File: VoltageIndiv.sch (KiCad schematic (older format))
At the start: 2 parts

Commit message: Placement canal passif intial
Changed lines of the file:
@@
 AR Path="/5F37413F/5EC90889" Ref="R79"  Part="1"
 AR Path="/5F374143/5EC90889" Ref="R81"  Part="1"
-F 0 "R81" H 5770 4046 50  0000 L CNN
+F 0 "R67" H 5770 4046 50  0000 L CNN
 F 1 "100k" H 5770 3955 50  0000 L CNN
 F 2 "Resistor_SMD:R_0805_2012Metric" V 5630 4000 50  0001 C CNN
@@
 AR Path="/5F37413F/5EC91EB2" Ref="R78"  Part="1"
 AR Path="/5F374143/5EC91EB2" Ref="R80"  Part="1"
-F 0 "R80" H 5770 3546 50  0000 L CNN
+F 0 "R66" H 5770 3546 50  0000 L CNN
 F 1 "43k" H 5770 3455 50  0000 L CNN
 F 2 "Resistor_SMD:R_0805_2012Metric" V 5630 3500 50  0001 C CNN
@@
 AR Path="/5F37413F/60F963CD" Ref="#PWR0138"  Part="1"
 AR Path="/5F374143/60F963CD" Ref="#PWR0139"  Part="1"
-F 0 "#PWR0139" H 5700 4050 50  0001 C CNN
+F 0 "#PWR0132" H 5700 4050 50  0001 C CNN
 F 1 "GNDA" H 5705 4127 50  0000 C CNN
 F 2 "" H 5700 4300 50  0001 C CNN

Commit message: Placement première charge active
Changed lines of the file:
@@
 $Descr A4 11693 8268
 encoding utf-8
-Sheet 35 80
+Sheet 41 80
 Title ""
 Date "2020-05-19"
@@
 AR Path="/5F37413F/5EC90889" Ref="R79"  Part="1"
 AR Path="/5F374143/5EC90889" Ref="R81"  Part="1"
-F 0 "R67" H 5770 4046 50  0000 L CNN
+F 0 "R81" H 5770 4046 50  0000 L CNN
 F 1 "100k" H 5770 3955 50  0000 L CNN
 F 2 "Resistor_SMD:R_0805_2012Metric" V 5630 4000 50  0001 C CNN
@@
 AR Path="/5F37413F/5EC91EB2" Ref="R78"  Part="1"
 AR Path="/5F374143/5EC91EB2" Ref="R80"  Part="1"
-F 0 "R66" H 5770 3546 50  0000 L CNN
+F 0 "R80" H 5770 3546 50  0000 L CNN
 F 1 "43k" H 5770 3455 50  0000 L CNN
 F 2 "Resistor_SMD:R_0805_2012Metric" V 5630 3500 50  0001 C CNN
@@
 AR Path="/5F37413F/60F963CD" Ref="#PWR0138"  Part="1"
 AR Path="/5F374143/60F963CD" Ref="#PWR0139"  Part="1"
-F 0 "#PWR0132" H 5700 4050 50  0001 C CNN
+F 0 "#PWR0139" H 5700 4050 50  0001 C CNN
 F 1 "GNDA" H 5705 4127 50  0000 C CNN
 F 2 "" H 5700 4300 50  0001 C CNN

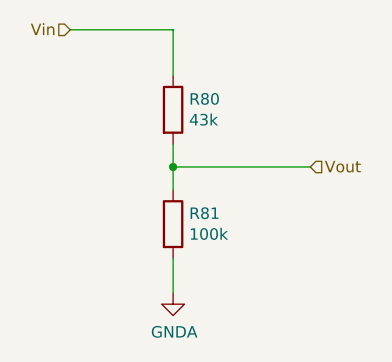
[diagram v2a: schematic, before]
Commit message: Placement première charge active 2nd try
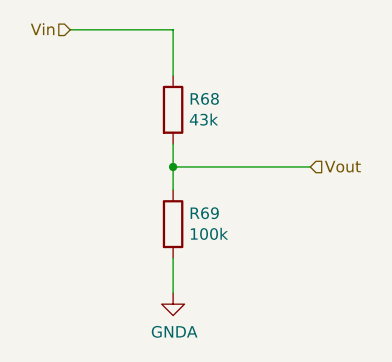
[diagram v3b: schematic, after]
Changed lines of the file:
@@
 $Descr A4 11693 8268
 encoding utf-8
-Sheet 41 80
+Sheet 36 80
 Title ""
 Date "2020-05-19"
@@
 AR Path="/5F37413F/5EC90889" Ref="R79"  Part="1"
 AR Path="/5F374143/5EC90889" Ref="R81"  Part="1"
-F 0 "R81" H 5770 4046 50  0000 L CNN
+F 0 "R69" H 5770 4046 50  0000 L CNN
 F 1 "100k" H 5770 3955 50  0000 L CNN
 F 2 "Resistor_SMD:R_0805_2012Metric" V 5630 4000 50  0001 C CNN
@@
 AR Path="/5F37413F/5EC91EB2" Ref="R78"  Part="1"
 AR Path="/5F374143/5EC91EB2" Ref="R80"  Part="1"
-F 0 "R80" H 5770 3546 50  0000 L CNN
+F 0 "R68" H 5770 3546 50  0000 L CNN
 F 1 "43k" H 5770 3455 50  0000 L CNN
 F 2 "Resistor_SMD:R_0805_2012Metric" V 5630 3500 50  0001 C CNN
@@
 AR Path="/5F37413F/60F963CD" Ref="#PWR0138"  Part="1"
 AR Path="/5F374143/60F963CD" Ref="#PWR0139"  Part="1"
-F 0 "#PWR0139" H 5700 4050 50  0001 C CNN
+F 0 "#PWR0133" H 5700 4050 50  0001 C CNN
 F 1 "GNDA" H 5705 4127 50  0000 C CNN
 F 2 "" H 5700 4300 50  0001 C CNN

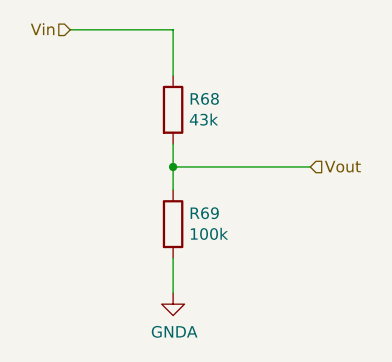
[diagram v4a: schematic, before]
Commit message: Petit ajustement pour accomoder le usb du arduino, pret pour routing
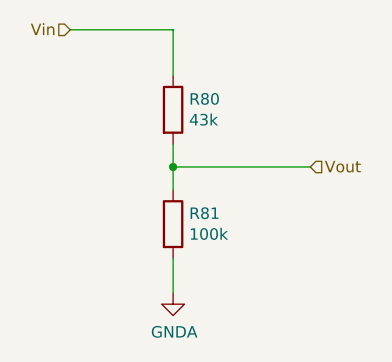
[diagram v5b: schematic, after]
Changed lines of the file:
@@
 AR Path="/5F37413F/5EC90889" Ref="R79"  Part="1"
 AR Path="/5F374143/5EC90889" Ref="R81"  Part="1"
-F 0 "R69" H 5770 4046 50  0000 L CNN
+F 0 "R81" H 5770 4046 50  0000 L CNN
 F 1 "100k" H 5770 3955 50  0000 L CNN
 F 2 "Resistor_SMD:R_0805_2012Metric" V 5630 4000 50  0001 C CNN
@@
 AR Path="/5F37413F/5EC91EB2" Ref="R78"  Part="1"
 AR Path="/5F374143/5EC91EB2" Ref="R80"  Part="1"
-F 0 "R68" H 5770 3546 50  0000 L CNN
+F 0 "R80" H 5770 3546 50  0000 L CNN
 F 1 "43k" H 5770 3455 50  0000 L CNN
 F 2 "Resistor_SMD:R_0805_2012Metric" V 5630 3500 50  0001 C CNN

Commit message: Debug routing
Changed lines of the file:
@@
 $Descr A4 11693 8268
 encoding utf-8
-Sheet 36 80
+Sheet 8 80
 Title ""
 Date "2020-05-19"
@@
 AR Path="/5F37413F/5EC90889" Ref="R79"  Part="1"
 AR Path="/5F374143/5EC90889" Ref="R81"  Part="1"
-F 0 "R81" H 5770 4046 50  0000 L CNN
+F 0 "R43" H 5770 4046 50  0000 L CNN
 F 1 "100k" H 5770 3955 50  0000 L CNN
 F 2 "Resistor_SMD:R_0805_2012Metric" V 5630 4000 50  0001 C CNN
@@
 AR Path="/5F37413F/5EC91EB2" Ref="R78"  Part="1"
 AR Path="/5F374143/5EC91EB2" Ref="R80"  Part="1"
-F 0 "R80" H 5770 3546 50  0000 L CNN
+F 0 "R42" H 5770 3546 50  0000 L CNN
 F 1 "43k" H 5770 3455 50  0000 L CNN
 F 2 "Resistor_SMD:R_0805_2012Metric" V 5630 3500 50  0001 C CNN
@@
 AR Path="/5F37413F/60F963CD" Ref="#PWR0138"  Part="1"
 AR Path="/5F374143/60F963CD" Ref="#PWR0139"  Part="1"
-F 0 "#PWR0139" H 5700 4050 50  0001 C CNN
+F 0 "#PWR055" H 5700 4050 50  0001 C CNN
 F 1 "GNDA" H 5705 4127 50  0000 C CNN
 F 2 "" H 5700 4300 50  0001 C CNN

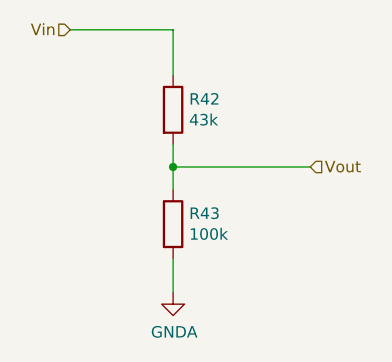
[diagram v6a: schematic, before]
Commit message: retrait des test points inutiles
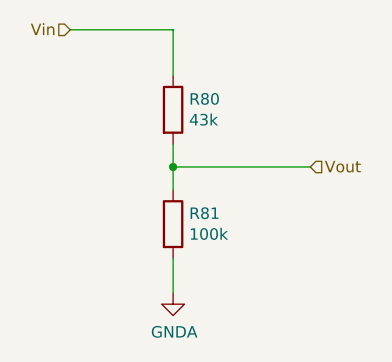
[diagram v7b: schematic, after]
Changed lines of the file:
@@
 AR Path="/5F37413F/5EC90889" Ref="R79"  Part="1"
 AR Path="/5F374143/5EC90889" Ref="R81"  Part="1"
-F 0 "R43" H 5770 4046 50  0000 L CNN
+F 0 "R81" H 5770 4046 50  0000 L CNN
 F 1 "100k" H 5770 3955 50  0000 L CNN
 F 2 "Resistor_SMD:R_0805_2012Metric" V 5630 4000 50  0001 C CNN
@@
 AR Path="/5F37413F/5EC91EB2" Ref="R78"  Part="1"
 AR Path="/5F374143/5EC91EB2" Ref="R80"  Part="1"
-F 0 "R42" H 5770 3546 50  0000 L CNN
+F 0 "R80" H 5770 3546 50  0000 L CNN
 F 1 "43k" H 5770 3455 50  0000 L CNN
 F 2 "Resistor_SMD:R_0805_2012Metric" V 5630 3500 50  0001 C CNN
@@
 AR Path="/5F37413F/60F963CD" Ref="#PWR0138"  Part="1"
 AR Path="/5F374143/60F963CD" Ref="#PWR0139"  Part="1"
-F 0 "#PWR055" H 5700 4050 50  0001 C CNN
+F 0 "#PWR0139" H 5700 4050 50  0001 C CNN
 F 1 "GNDA" H 5705 4127 50  0000 C CNN
 F 2 "" H 5700 4300 50  0001 C CNN

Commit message: Routed most of the power
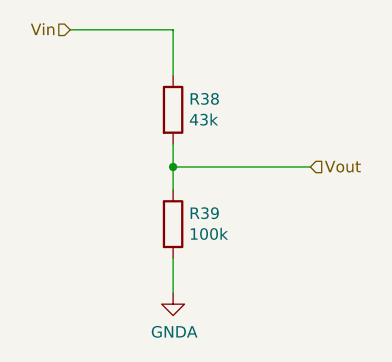
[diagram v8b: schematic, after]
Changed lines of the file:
@@
 $Descr A4 11693 8268
 encoding utf-8
-Sheet 8 80
+Sheet 6 80
 Title ""
 Date "2020-05-19"
@@
 AR Path="/5F37413F/5EC90889" Ref="R79"  Part="1"
 AR Path="/5F374143/5EC90889" Ref="R81"  Part="1"
-F 0 "R81" H 5770 4046 50  0000 L CNN
+F 0 "R39" H 5770 4046 50  0000 L CNN
 F 1 "100k" H 5770 3955 50  0000 L CNN
 F 2 "Resistor_SMD:R_0805_2012Metric" V 5630 4000 50  0001 C CNN
@@
 AR Path="/5F37413F/5EC91EB2" Ref="R78"  Part="1"
 AR Path="/5F374143/5EC91EB2" Ref="R80"  Part="1"
-F 0 "R80" H 5770 3546 50  0000 L CNN
+F 0 "R38" H 5770 3546 50  0000 L CNN
 F 1 "43k" H 5770 3455 50  0000 L CNN
 F 2 "Resistor_SMD:R_0805_2012Metric" V 5630 3500 50  0001 C CNN
@@
 AR Path="/5F37413F/60F963CD" Ref="#PWR0138"  Part="1"
 AR Path="/5F374143/60F963CD" Ref="#PWR0139"  Part="1"
-F 0 "#PWR0139" H 5700 4050 50  0001 C CNN
+F 0 "#PWR053" H 5700 4050 50  0001 C CNN
 F 1 "GNDA" H 5705 4127 50  0000 C CNN
 F 2 "" H 5700 4300 50  0001 C CNN
